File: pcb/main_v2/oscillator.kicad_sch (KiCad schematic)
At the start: 23 parts, among them IC501 SPF5043Z, IC502 PD0922J5050S2HF, IC503 SPF5043Z, U501 XMB0220K1-50100G, Y501 ASGTX-P-1.500GHZ-1

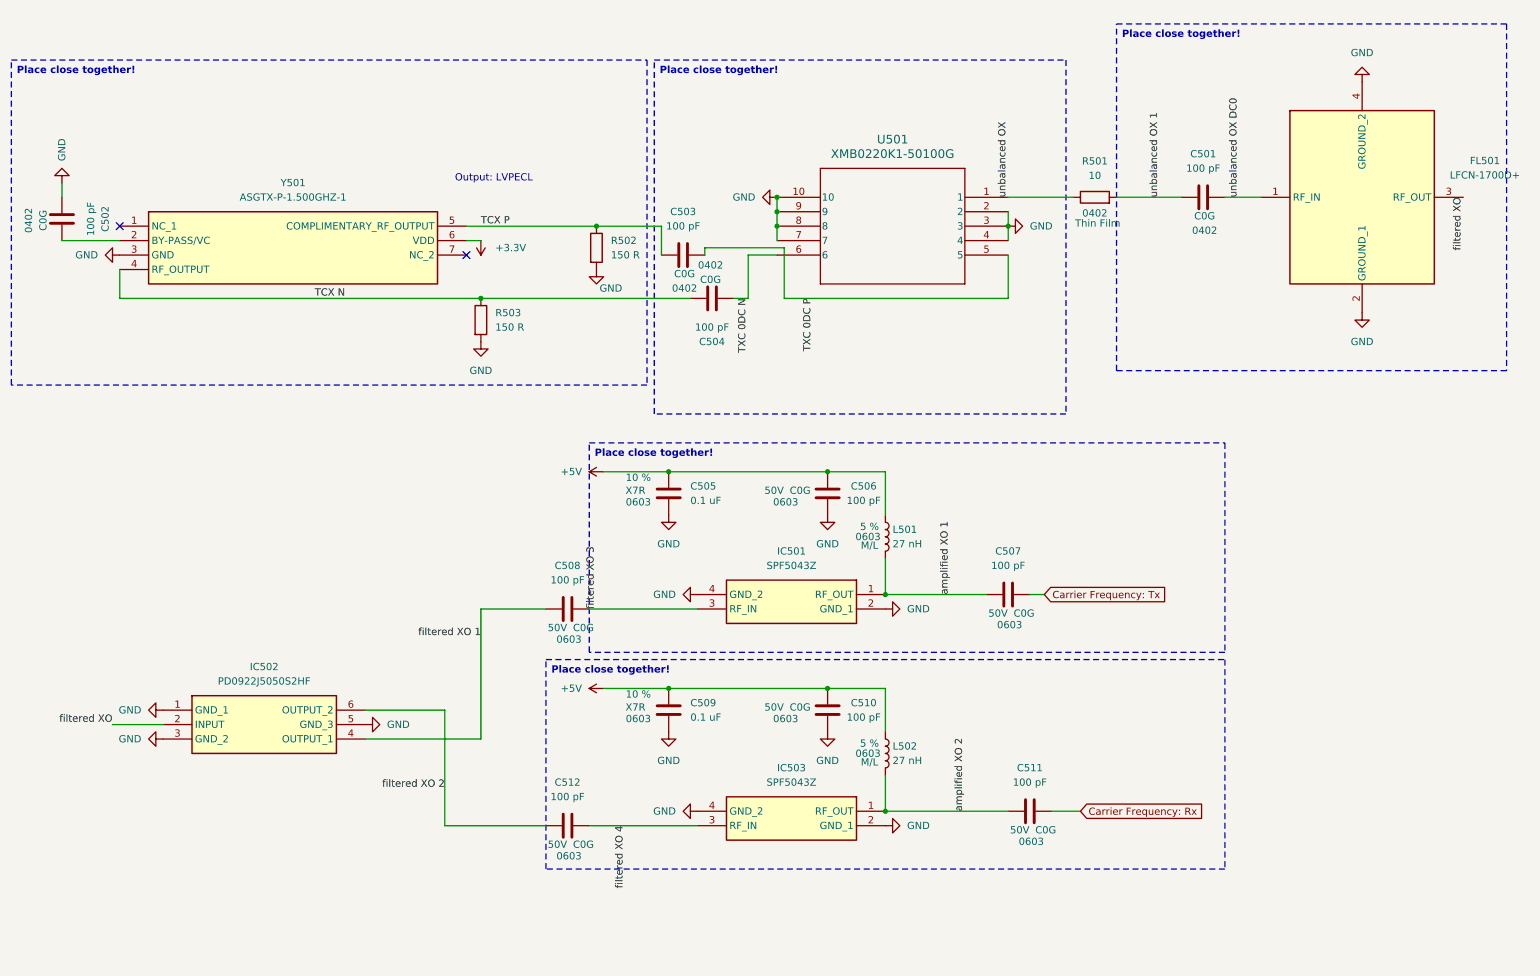
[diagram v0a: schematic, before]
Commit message: updated layout
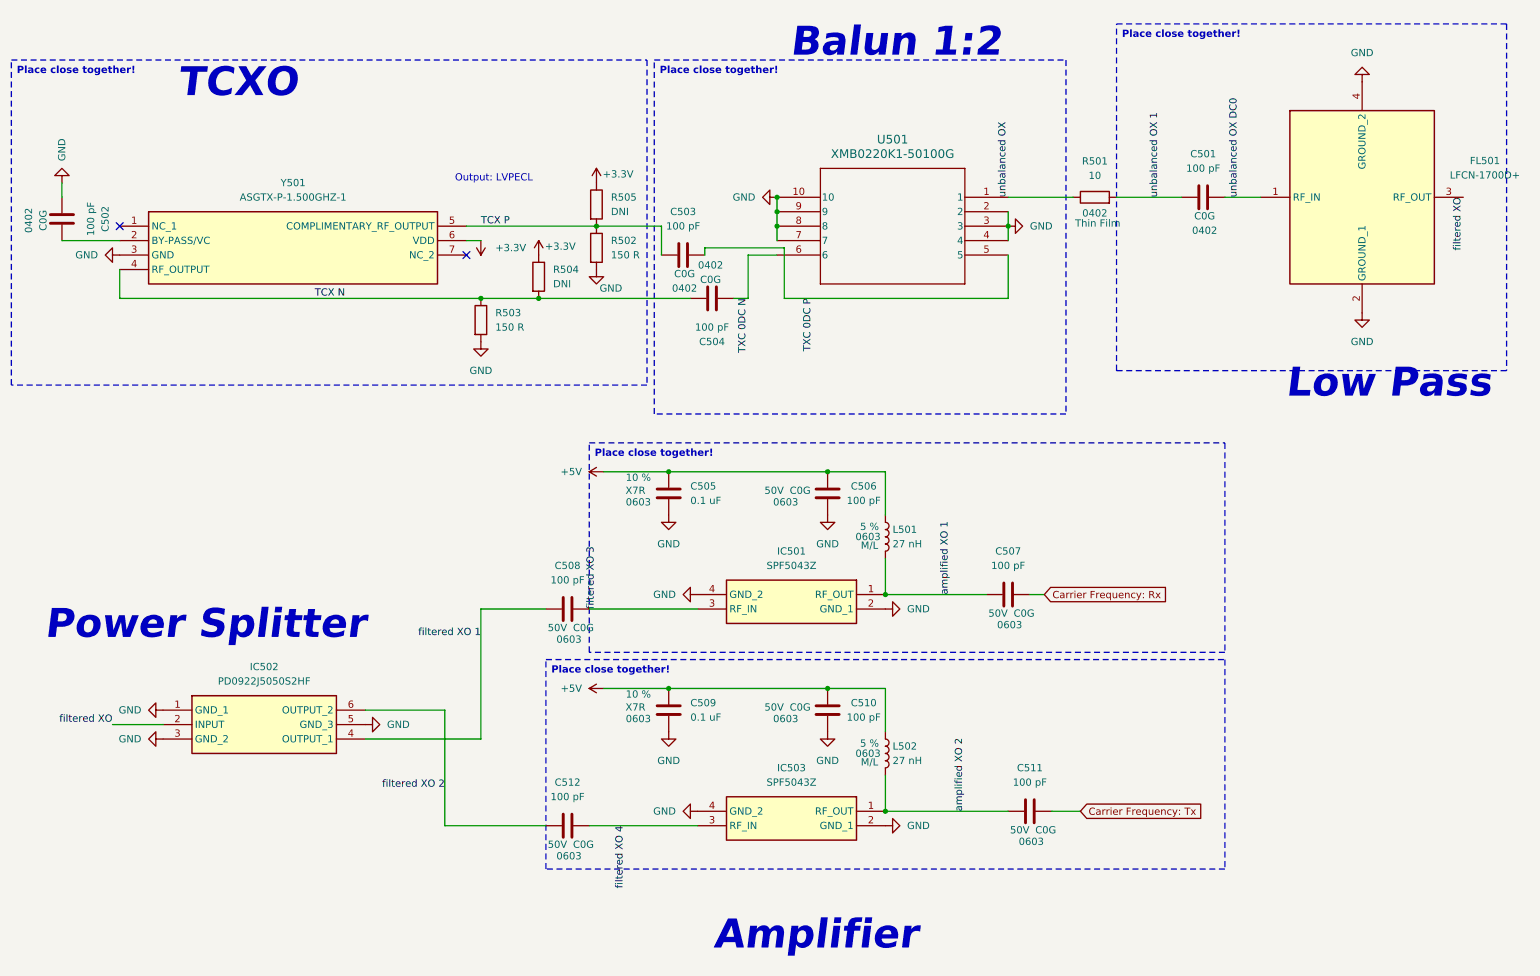
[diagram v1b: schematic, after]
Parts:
- added R504, R505: DNI, Resistor_SMD:R_0603_1608Metric, symbol Device:R
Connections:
- net +3.3V: now also R504.1, R505.1
- net Carrier Frequency: Rx: now also C507.1; no longer C511.1
- net Carrier Frequency: Tx: now also C511.1; no longer C507.1
- net TCX N: now also R504.2
- net TCX P: now also R505.2
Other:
- note added: "Amplifier"
- note added: "Balun 1:2"
- note added: "Low Pass"
- note added: "Power Splitter"
- note added: "TCXO"
